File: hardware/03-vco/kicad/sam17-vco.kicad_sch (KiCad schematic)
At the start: 23 parts, among them J1 PSU +12/G/G/-12, U11 L78L05, U12 LD1117S33TR, U8 ADR4525

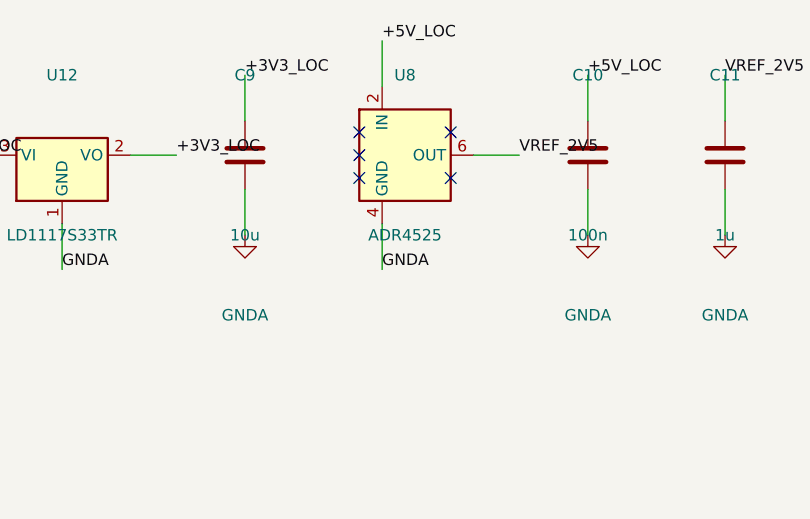
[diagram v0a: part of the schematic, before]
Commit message: Modulo 3 VCO: fix de revision, Value de U8 lleva el grado (ADR4525BRZ)
El "OJO: es ADR4525" del contexto de despacho corregia el lib_id del
simbolo, no el Value. El Value es donde el repo registra la pieza exacta a
comprar, y el grado importa: el spec dice que el grado A revienta el
presupuesto de afinacion. Mismo precedente que modulo 2 (AD5686RBRUZ,
TL074H conservan su sufijo en Value aunque el lib_id sea generico).

lib_id sin tocar (Reference_Voltage:ADR4525, resuelve bien el simbolo).
Guardias verdes, ERC identico: 0 errores, 8 avisos esperados
(isolated_pin_label en los TP huerfanos de CV_PITCH/MIXO).

Co-Authored-By: Claude Fable 5 <noreply@anthropic.com>
Claude-Session: https://claude.ai/code/session_01TtD4jRd4wyRdkyuChqdVe2
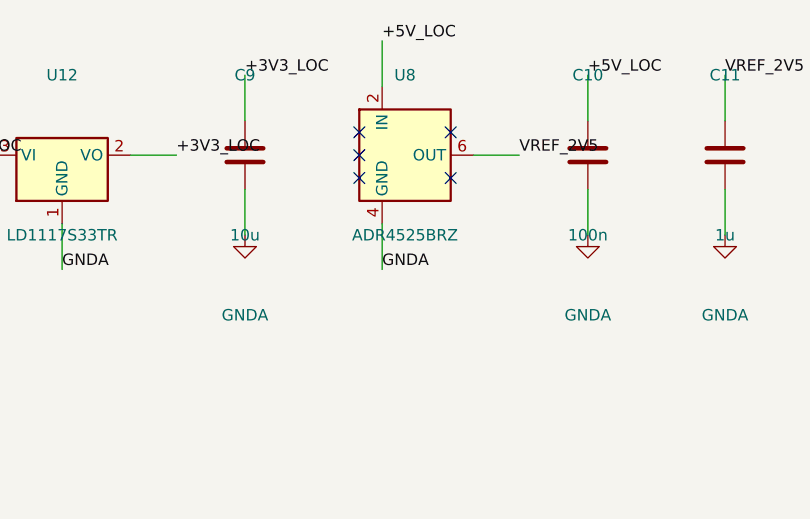
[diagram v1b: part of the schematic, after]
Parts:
- U8: value ADR4525 -> ADR4525BRZ
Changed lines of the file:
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@@
 			)
 		)
-		(property "Value" "ADR4525"
+		(property "Value" "ADR4525BRZ"
 			(at 190.5 34.29 0)
 			(show_name no)

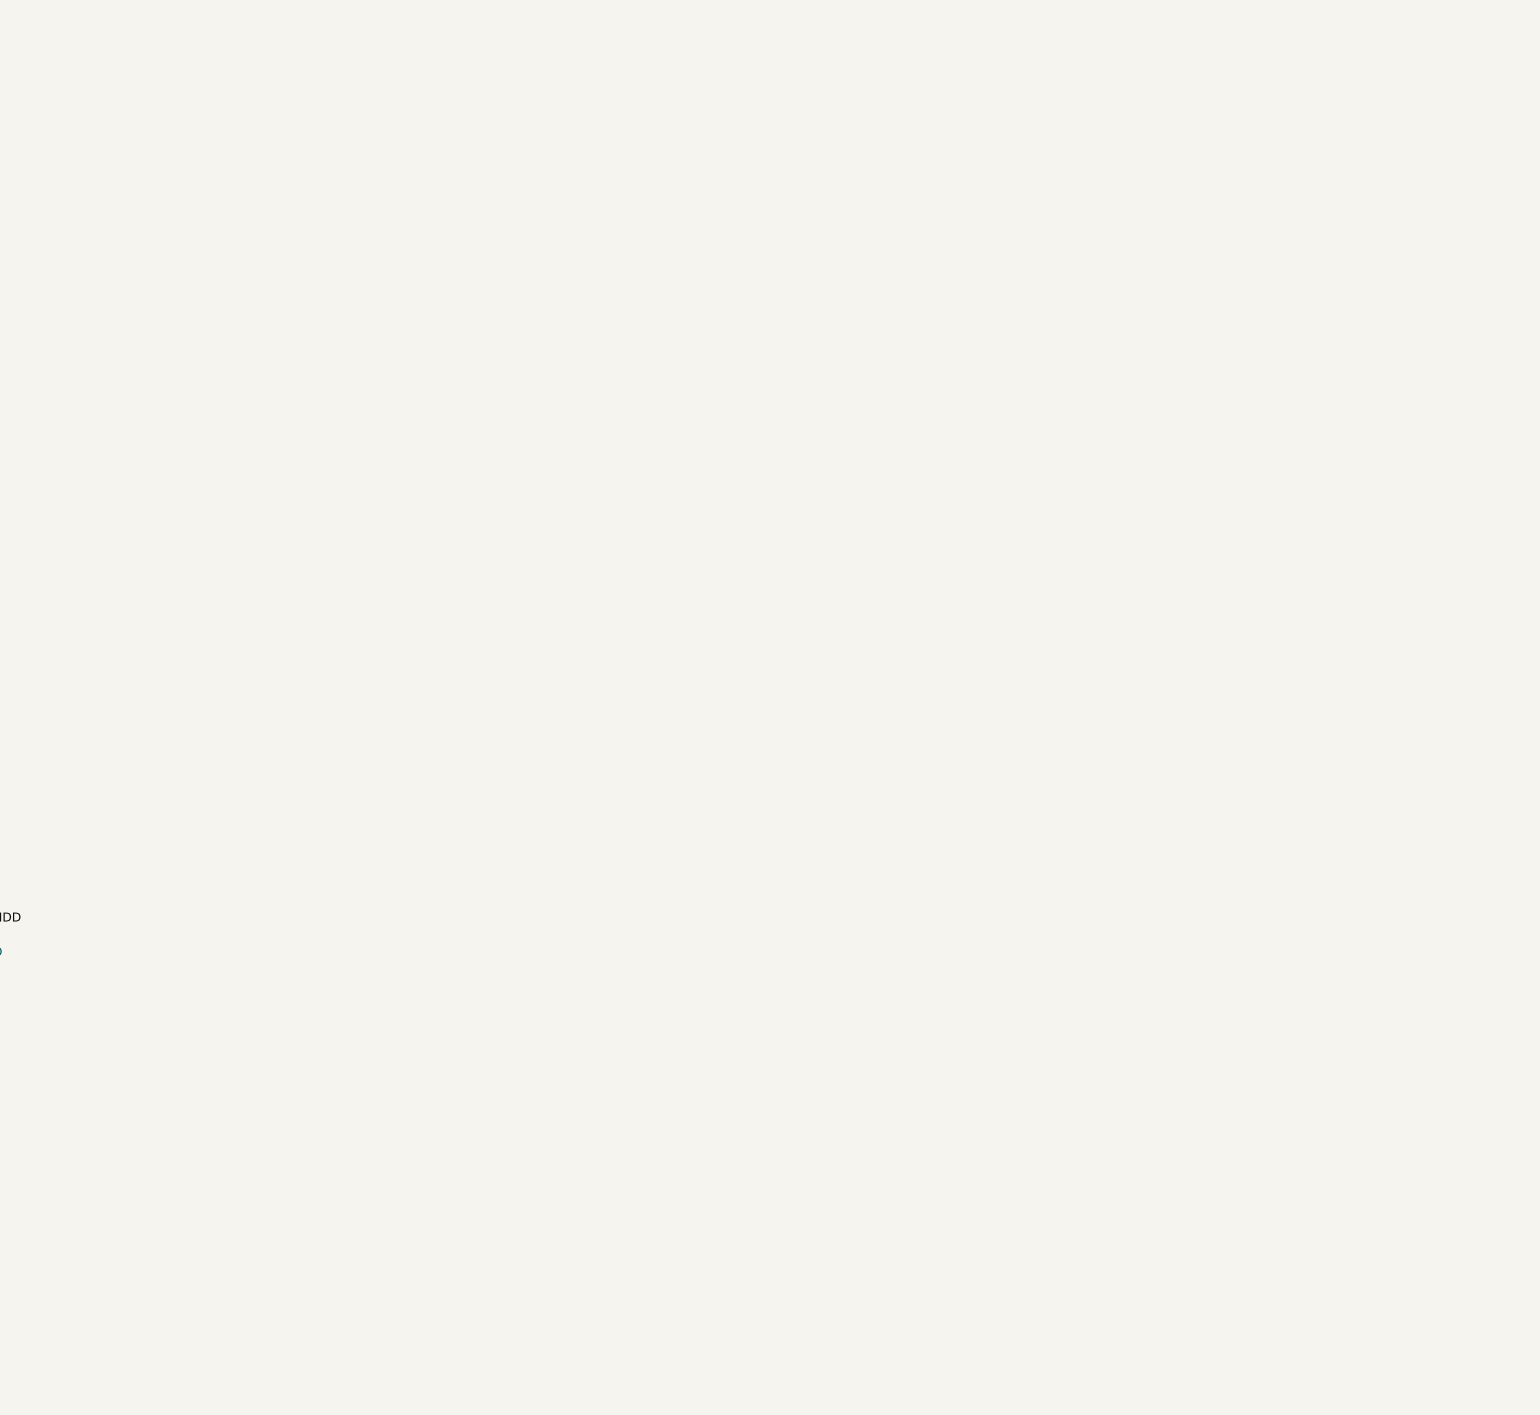
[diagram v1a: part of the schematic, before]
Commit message: Modulo 3 VCO: bloque digital -- cadena de 3 DAC, 74HC14, telemetria I2C y J2
Tarea 3: extiende build_schematic.py (no lo reescribe) con bloque_digital()
-- bloque_dac() (U5-U7 AD5686R en cadena soldada DCEN, GAIN=x1/LDAC/RSTSEL
igual que el modulo 2, RESET atado a +3V3_LOC por no haber GPIO de reset en
esta placa), bloque_hc14() (U10, Schmitt trigger multi-unidad para
TUNE_OUT_1..4), bloque_telemetria() (U13 TMP1075 direccion 0, U14 EEPROM,
pullups I2C) y bloque_mazo() (J2 IDC 2x6 con el contrato del enlace, dejado
tambien como tabla comentada J2_PINOUT para los modulos 5-7).

Fix de paso: el pin 5 de la EEPROM (24AA02E-OT) es no_connect en el propio
simbolo -- igual que el EP del SSI2130 en la Tarea 1 -- y ponerle la cruz de
no-conexion de bloque() disparaba no_connect_dangling en el ERC; se cablea
a mano sin tocar ese pin.

ERC: 20 avisos (4 error pin_not_driven + 16 warning), todos sobre redes que
esta tarea deja deliberadamente pendientes para la Tarea 4 (SQ_1..4,
PWM_CV/MIX_*) o son permanentes y benignos (VREF_2V5 bidireccional/power
output). Detalle completo en el reporte de la tarea.

Co-Authored-By: Claude Fable 5 <noreply@anthropic.com>
Claude-Session: https://claude.ai/code/session_01TtD4jRd4wyRdkyuChqdVe2
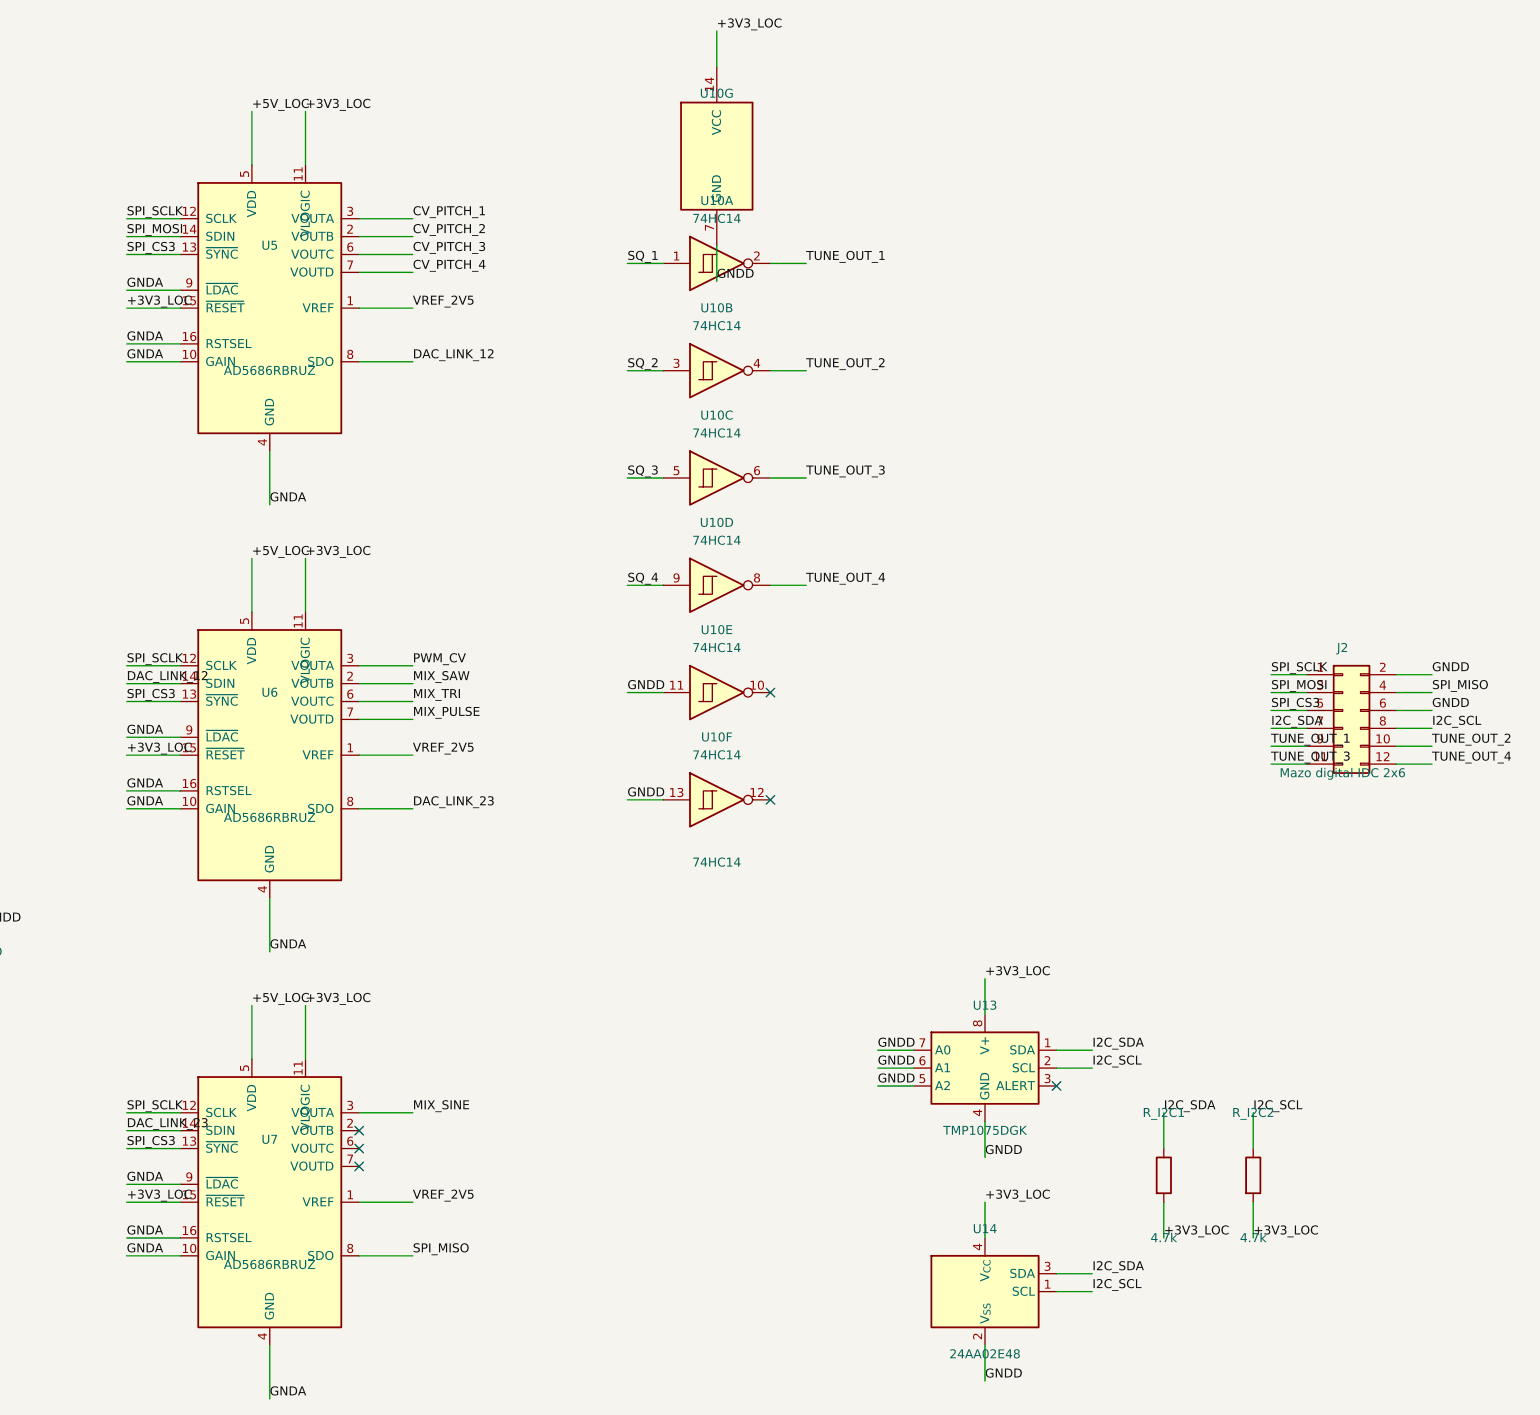
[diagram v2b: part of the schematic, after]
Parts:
- added J2: Mazo digital IDC 2x6, Connector_IDC:IDC-Header_2x06_P2.54mm_Vertical, symbol Connector_Generic:Conn_02x06_Odd_Even
- added R_I2C1, R_I2C2: 4.7k, Resistor_SMD:R_0805_2012Metric, symbol Device:R
- added U10: 74HC14, Package_SO:SOIC-14_3.9x8.7mm_P1.27mm, symbol 74xx:74HC14
- added U13: TMP1075DGK, Package_SO:VSSOP-8_3x3mm_P0.65mm, symbol Sensor_Temperature:TMP1075DGK
- added U14: 24AA02E48, Package_TO_SOT_SMD:SOT-23-5, symbol Memory_EEPROM:24AA02E-OT
- added U5, U6, U7: AD5686RBRUZ, Package_SO:TSSOP-16_4.4x5mm_P0.65mm, symbol sam17:AD5686RBRUZ
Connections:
- net +3V3_LOC: now also R_I2C1.2, R_I2C2.2, U10.14 (VCC), U13.8 (V+), U14.4 (V_{CC}), U5.11 (VLOGIC), U5.15 (~{RESET}), U6.11 (VLOGIC), U6.15 (~{RESET}), U7.11 (VLOGIC), U7.15 (~{RESET})
- net +5V_LOC: now also U5.5 (VDD), U6.5 (VDD), U7.5 (VDD)
- net CV_PITCH_1: now also U5.3 (VOUTA)
- net CV_PITCH_2: now also U5.2 (VOUTB)
- net CV_PITCH_3: now also U5.6 (VOUTC)
- net CV_PITCH_4: now also U5.7 (VOUTD)
- net GNDA: now also U5.10 (GAIN), U5.16 (RSTSEL), U5.4 (GND), U5.9 (~{LDAC}), U6.10 (GAIN), U6.16 (RSTSEL), U6.4 (GND), U6.9 (~{LDAC}), U7.10 (GAIN), U7.16 (RSTSEL), U7.4 (GND), U7.9 (~{LDAC})
- net GNDD: now also J2.2 (Pin_2), J2.6 (Pin_6), U10.11, U10.13, U10.7 (GND), U13.4 (GND), U13.5 (A2), U13.6 (A1), U13.7 (A0), U14.2 (V_{SS})
- net VREF_2V5: now also U5.1 (VREF), U6.1 (VREF), U7.1 (VREF)
- new net DAC_LINK_12: U5.8 (SDO), U6.14 (SDIN)
- new net DAC_LINK_23: U6.8 (SDO), U7.14 (SDIN)
- new net I2C_SCL: J2.8 (Pin_8), R_I2C2.1, U13.2 (SCL), U14.1 (SCL)
- new net I2C_SDA: J2.7 (Pin_7), R_I2C1.1, U13.1 (SDA), U14.3 (SDA)
- new net MIX_PULSE: U6.7 (VOUTD)
- new net MIX_SAW: U6.2 (VOUTB)
- new net MIX_SINE: U7.3 (VOUTA)
- new net MIX_TRI: U6.6 (VOUTC)
- new net PWM_CV: U6.3 (VOUTA)
- new net SPI_CS3: J2.5 (Pin_5), U5.13 (~{SYNC}), U6.13 (~{SYNC}), U7.13 (~{SYNC})
- new net SPI_MISO: J2.4 (Pin_4), U7.8 (SDO)
- new net SPI_MOSI: J2.3 (Pin_3), U5.14 (SDIN)
- new net SPI_SCLK: J2.1 (Pin_1), U5.12 (SCLK), U6.12 (SCLK), U7.12 (SCLK)
- new net SQ_1: U10.1
- new net SQ_2: U10.3
- new net SQ_3: U10.5
- new net SQ_4: U10.9
- new net TUNE_OUT_1: J2.9 (Pin_9), U10.2
- new net TUNE_OUT_2: J2.10 (Pin_10), U10.4
- new net TUNE_OUT_3: J2.11 (Pin_11), U10.6
- new net TUNE_OUT_4: J2.12 (Pin_12), U10.8
- no-connect marks 5 -> 11
